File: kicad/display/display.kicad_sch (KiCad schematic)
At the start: 25 parts, among them J1 Conn. 02x12, P1 10k, P2 10k, P3 10k stereo, P4 10k, T1 2N3904, T2 2N3904, U1 4066N, U2 RC1602A

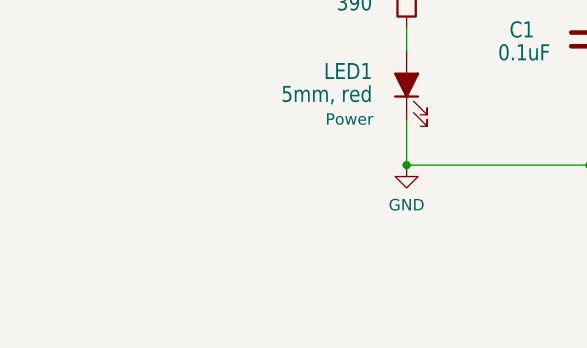
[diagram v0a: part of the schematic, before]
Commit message: Fixing mounting holes for display print
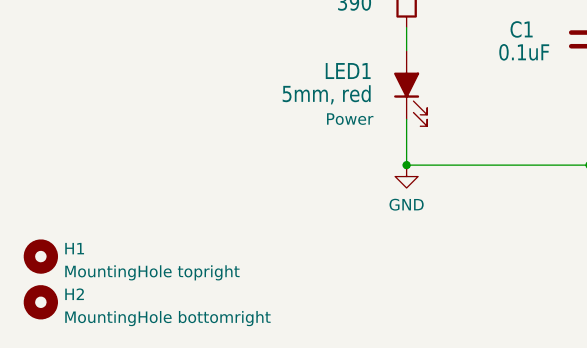
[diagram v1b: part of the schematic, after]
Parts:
- added H1: MountingHole topright, MountingHole:MountingHole_2.1mm, symbol Mechanical:MountingHole
- added H2: MountingHole bottomright, MountingHole:MountingHole_2.1mm, symbol Mechanical:MountingHole
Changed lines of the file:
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@@
     (pin "4")
+  )
+  (symbol (lib_id "Mechanical:MountingHole") (at 24.13 187.96 0) (unit 1)
+    (in_bom yes) (on_board yes) (fields_autoplaced)
+    (property "Reference" "H1" (id 0) (at 26.67 187.1253 0)
+      (effects (font (size 1.27 1.27)) (justify left))
+    )
+    (property "Value" "MountingHole topright" (id 1) (at 26.67 189.6622 0)
+      (effects (font (size 1.27 1.27)) (justify left))
+    )
+    (property "Footprint" "MountingHole:MountingHole_2.1mm" (id 2) (at 24.13 187.96 0)
+      (effects (font (size 1.27 1.27)) hide)
+    )
+    (property "Datasheet" "~" (id 3) (at 24.13 187.96 0)
+      (effects (font (size 1.27 1.27)) hide)
+    )
   )
   (symbol (lib_id "Device:R_Potentiometer") (at 41.91 107.95 0) (mirror x) (unit 1)
@@
     (pin "3")
     (pin "4")
+  )
+  (symbol (lib_id "Mechanical:MountingHole") (at 24.13 193.04 0) (unit 1)
+    (in_bom yes) (on_board yes) (fields_autoplaced)
+    (property "Reference" "H2" (id 0) (at 26.67 192.2053 0)
+      (effects (font (size 1.27 1.27)) (justify left))
+    )
+    (property "Value" "MountingHole bottomright" (id 1) (at 26.67 194.7422 0)
+      (effects (font (size 1.27 1.27)) (justify left))
+    )
+    (property "Footprint" "MountingHole:MountingHole_2.1mm" (id 2) (at 24.13 193.04 0)
+      (effects (font (size 1.27 1.27)) hide)
+    )
+    (property "Datasheet" "~" (id 3) (at 24.13 193.04 0)
+      (effects (font (size 1.27 1.27)) hide)
+    )
   )
   (symbol (lib_id "Device:R") (at 242.57 33.02 0) (mirror x) (unit 1)
@@
       (reference "C1") (unit 1) (value "0.1uF") (footprint "Capacitor_THT:C_Disc_D3.4mm_W2.1mm_P2.50mm")
     )
+    (path "/52fbbb5e-e2d2-42c1-a80c-566ffb9e6372"
+      (reference "H1") (unit 1) (value "MountingHole topright") (footprint "MountingHole:MountingHole_2.1mm")
+    )
+    (path "/a2ed2906-2e6a-49f5-b00c-a2101572ab11"
+      (reference "H2") (unit 1) (value "MountingHole bottomright") (footprint "MountingHole:MountingHole_2.1mm")
+    )
     (path "/e5041354-b711-4490-a712-dc956e45a881"

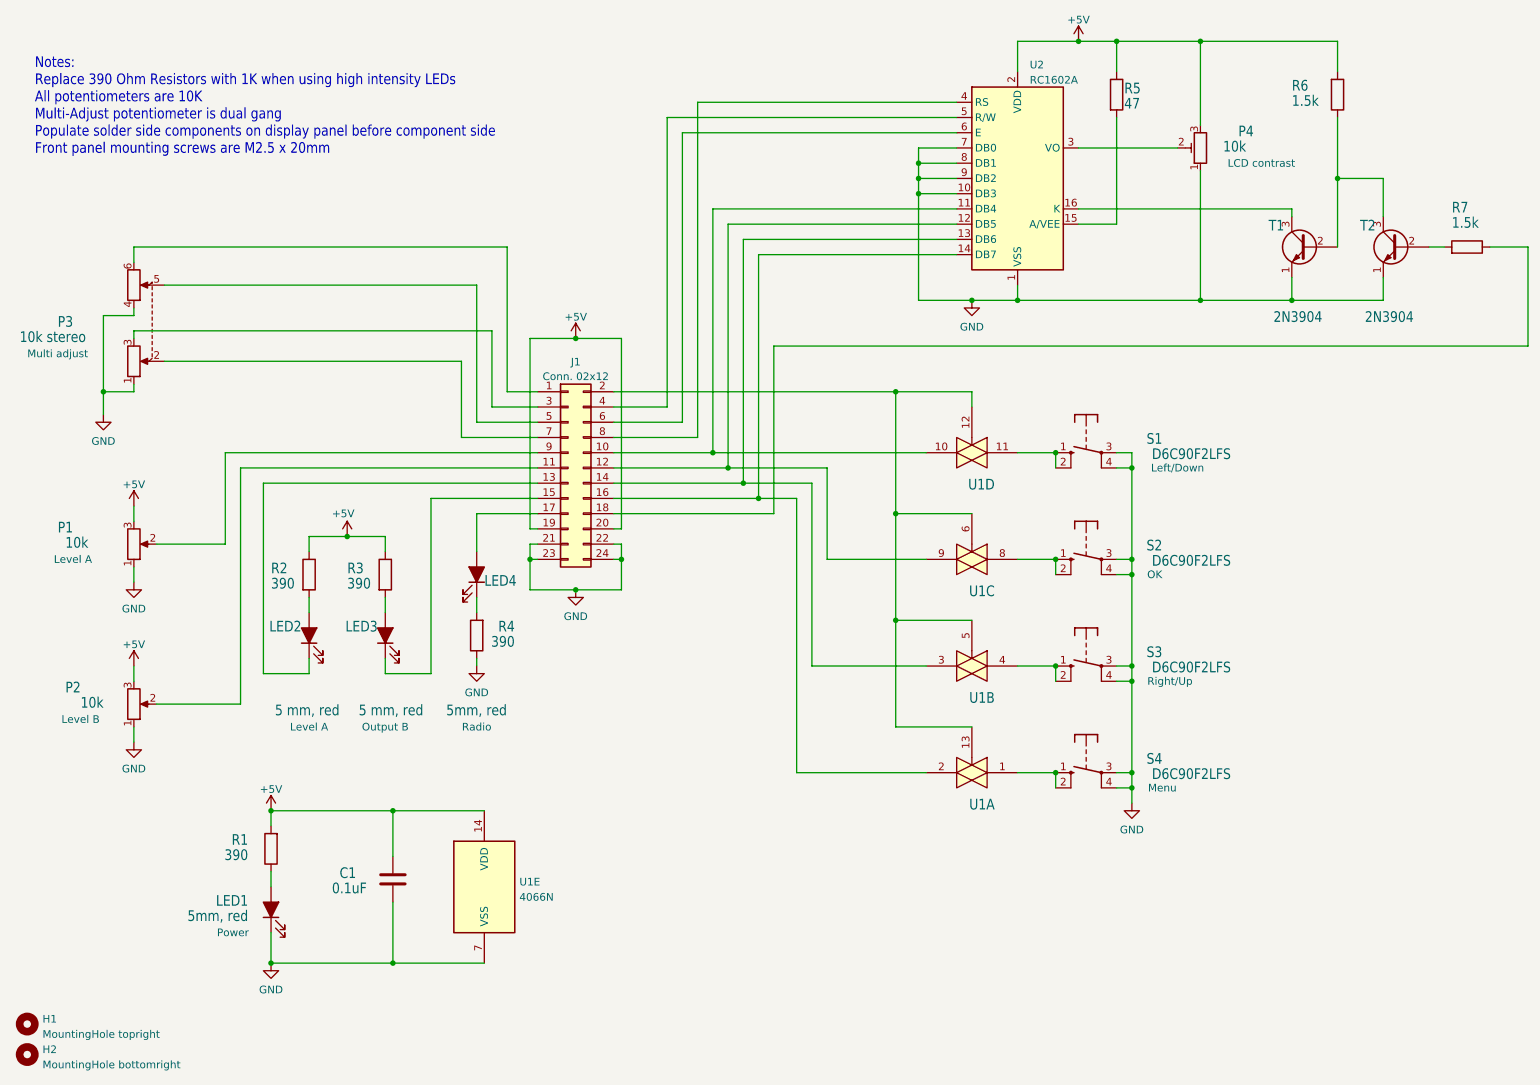
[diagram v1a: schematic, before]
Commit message: Display print is now on parity with V1.4, but has been re-routed. U3 has also been rotated 180 degrees. Some components have been moved to other places as well
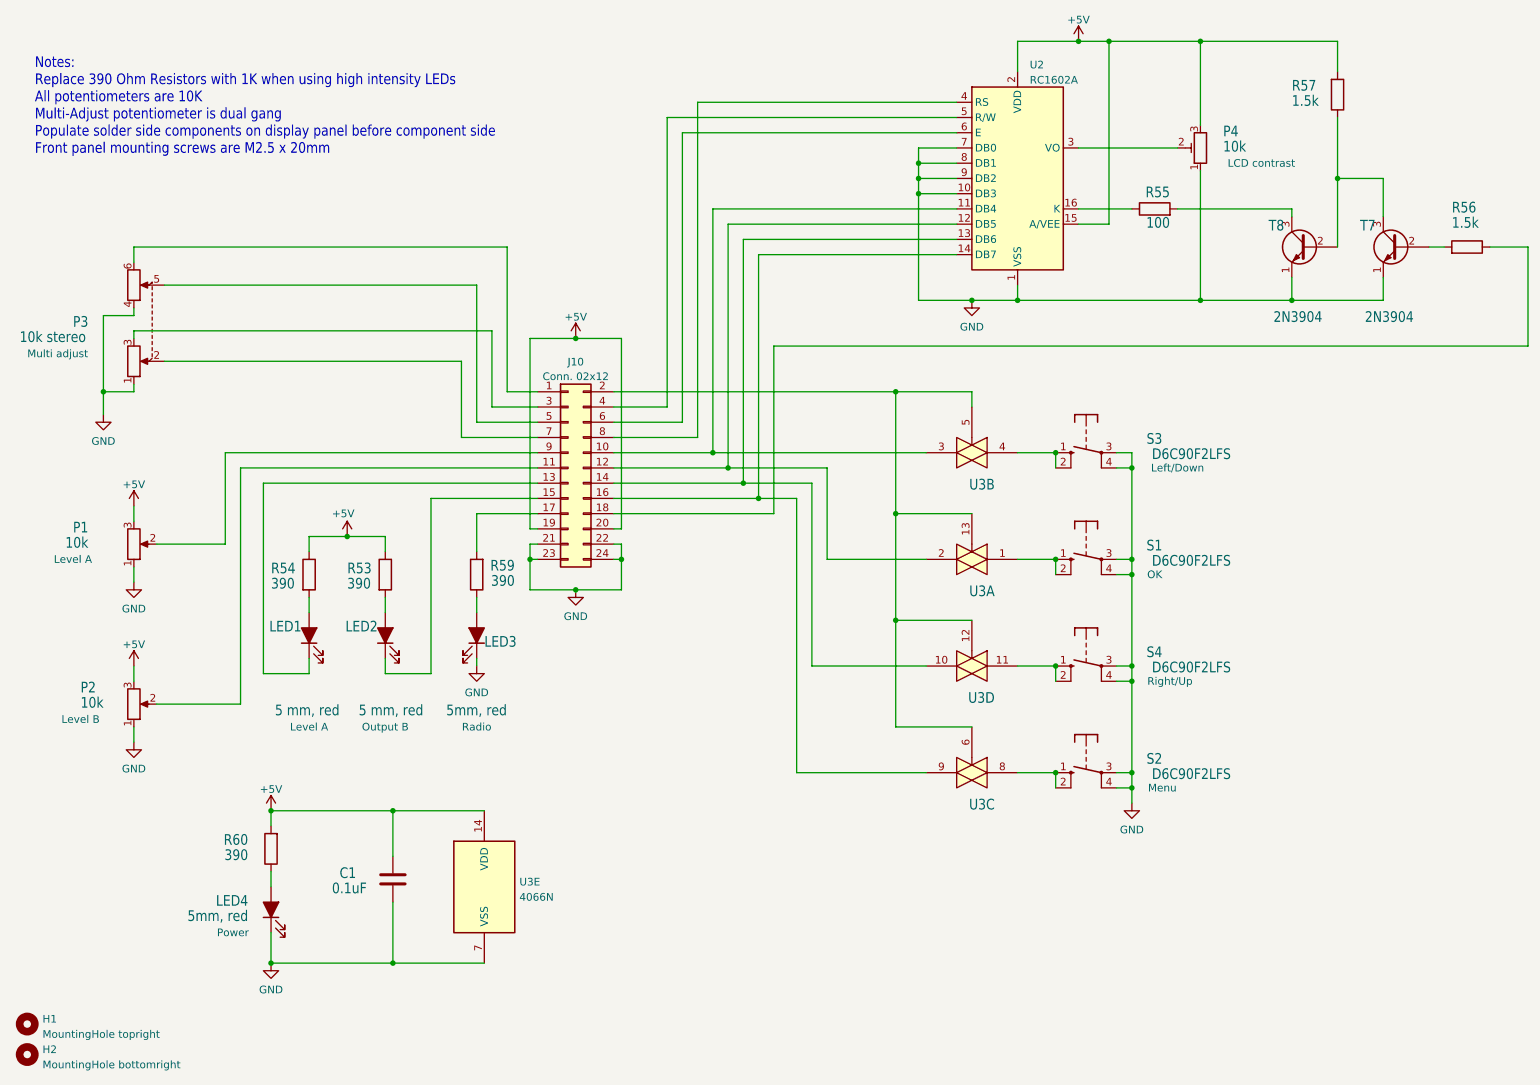
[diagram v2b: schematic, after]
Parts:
- R55: renamed from R5; value 47 -> 100
- renumbered J1 to J10, LED2 to LED1, LED3 to LED2, LED4 to LED3, LED1 to LED4, R3 to R53, R2 to R54, R7 to R56, R6 to R57, R4 to R59, R1 to R60, S2 to S1, S4 to S2, S1 to S3, S3 to S4, T2 to T7, T1 to T8, U1 to U3
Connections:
- net +5V: now also U2.15 (A/VEE); no longer R55.1
- net GND: now also LED3.1 (K); no longer R59.1
- net at R59.2: now also J10.17 (Pin_17); no longer LED3.1 (K)
- net at R55.2: now also T8.3 (C); no longer U2.15 (A/VEE)
- net at J10.10 (Pin_10), U2.11 (DB4): now also U3.3; no longer U3.10
- net at J10.12 (Pin_12), U2.12 (DB5): now also U3.2; no longer U3.9
- net at J10.14 (Pin_14), U2.13 (DB6): now also U3.10; no longer U3.3
- net at J10.16 (Pin_16), U2.14 (DB7): now also U3.9; no longer U3.2
- net at U2.16 (K): now also R55.1; no longer T8.3 (C)
- net at S4.1 (S), S4.2 (S@1): now also U3.11; no longer U3.4
- net at S1.1 (S), S1.2 (S@1): now also U3.1; no longer U3.8
- net at S2.1 (S), S2.2 (S@1): now also U3.8; no longer U3.1
- net at LED3.2 (A): now also R59.1; no longer J10.17 (Pin_17)
- net at S3.1 (S), S3.2 (S@1): now also U3.4; no longer U3.11
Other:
- title: MK-312 Display print -> MK-312BT Display print
- moved on the sheet: LED3, R55, R59, U3A, U3B, U3C, U3D

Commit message: Brought component numbers back in line with the original schematics
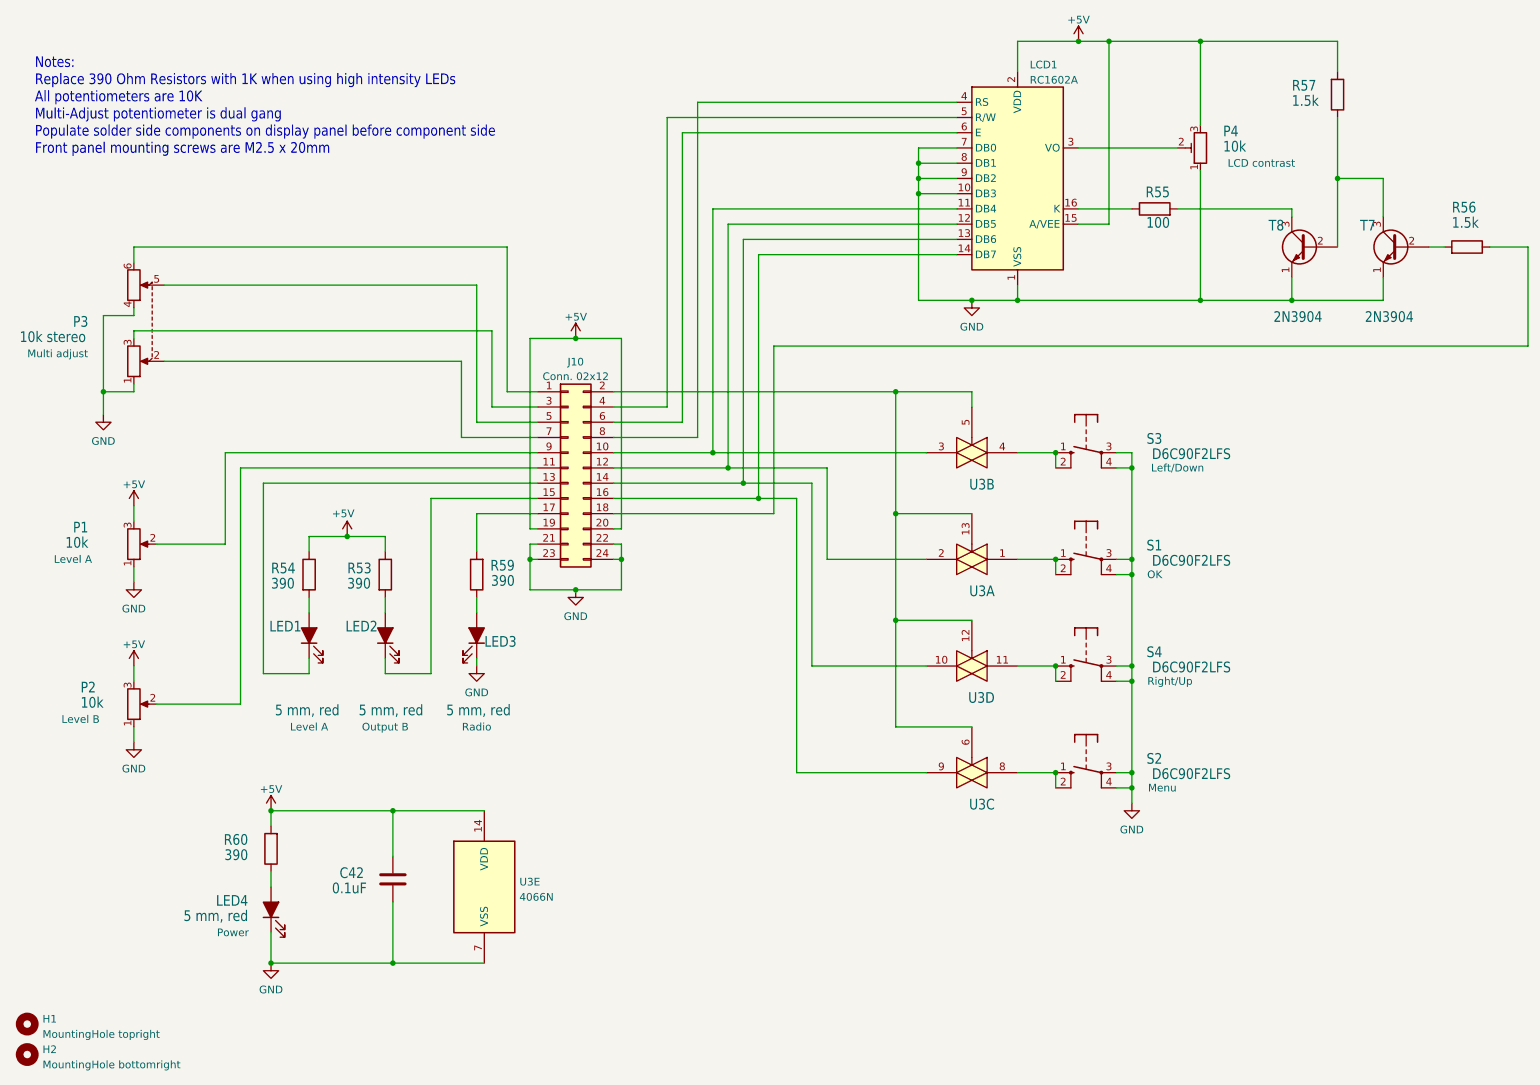
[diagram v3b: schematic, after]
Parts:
- LED3, LED4: value 5mm, red -> 5 mm, red
- renumbered C1 to C42, U2 to LCD1
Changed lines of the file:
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@@
   (symbol (lib_id "Device:C") (at 85.09 163.83 0) (unit 1)
     (in_bom yes) (on_board yes)
-    (property "Reference" "C1" (id 0) (at 76.2 163.83 0)
+    (property "Reference" "C42" (id 0) (at 76.2 163.83 0)
       (effects (font (size 1.778 1.5113)) (justify left bottom))
     )
@@
   (symbol (lib_id "Display_Character:RC1602A") (at 189.23 46.99 0) (unit 1)
     (in_bom yes) (on_board yes) (fields_autoplaced)
-    (property "Reference" "U2" (id 0) (at 191.2494 28.0502 0)
+    (property "Reference" "LCD1" (id 0) (at 191.2494 28.0502 0)
       (effects (font (size 1.27 1.27)) (justify left))
     )
@@
       (effects (font (size 1.778 1.5113)) (justify left bottom))
     )
-    (property "Value" "5mm, red" (id 1) (at 60.96 168.91 90)
+    (property "Value" "5 mm, red" (id 1) (at 60.96 168.91 90)
       (effects (font (size 1.778 1.5113)) (justify left bottom))
     )
@@
       (effects (font (size 1.778 1.5113)) (justify left bottom))
     )
-    (property "Value" "5mm, red" (id 1) (at 93.98 134.62 90)
+    (property "Value" "5 mm, red" (id 1) (at 93.98 134.62 90)
       (effects (font (size 1.778 1.5113)) (justify left bottom))
     )
@@
     )
     (path "/37d05d0c-fd2c-47ad-99b1-bd0042f10a5e"
-      (reference "C1") (unit 1) (value "0.1uF") (footprint "Capacitor_THT:C_Disc_D3.4mm_W2.1mm_P2.50mm")
+      (reference "C42") (unit 1) (value "0.1uF") (footprint "Capacitor_THT:C_Disc_D3.4mm_W2.1mm_P2.50mm")
     )
     (path "/52fbbb5e-e2d2-42c1-a80c-566ffb9e6372"
@@
       (reference "J10") (unit 1) (value "Conn. 02x12") (footprint "Connector_IDC:IDC-Header_2x12_P2.54mm_Vertical")
     )
+    (path "/49ff3ae1-ae02-4def-bf64-4b538d23f00c"
+      (reference "LCD1") (unit 1) (value "RC1602A") (footprint "Display:WC1602A")
+    )
     (path "/e5b8127c-a986-441d-9655-260089edadc4"
       (reference "LED1") (unit 1) (value "5 mm, red") (footprint "LED_THT:LED_D5.0mm")
@@
     )
     (path "/7f11bb71-0b23-427a-a835-54b1dd9e05f6"
-      (reference "LED3") (unit 1) (value "5mm, red") (footprint "LED_THT:LED_D5.0mm")
+      (reference "LED3") (unit 1) (value "5 mm, red") (footprint "LED_THT:LED_D5.0mm")
     )
     (path "/5a196dae-b249-4e08-89df-c3de0945af88"
-      (reference "LED4") (unit 1) (value "5mm, red") (footprint "LED_THT:LED_D5.0mm")
+      (reference "LED4") (unit 1) (value "5 mm, red") (footprint "LED_THT:LED_D5.0mm")
     )
     (path "/566b906f-57c5-4d05-84c1-6fa6c729218f"
@@
       (reference "T8") (unit 1) (value "2N3904") (footprint "Package_TO_SOT_THT:TO-92_Inline")
     )
-    (path "/49ff3ae1-ae02-4def-bf64-4b538d23f00c"
-      (reference "U2") (unit 1) (value "RC1602A") (footprint "Display:WC1602A")
-    )
     (path "/73fcf29c-182d-4f9a-9237-8fd20f0b67be"

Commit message: Two small fixups for the display & frontend. Made mounting holes in display PCB larger. Moved LCD window slightly to the right on the front panel.
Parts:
- H1, H2: footprint MountingHole:MountingHole_2.1mm -> MountingHole:MountingHole_2.5mm
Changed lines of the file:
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@@
   (title_block
     (title "MK-312BT Display print")
-    (date "2022-08-09")
-    (rev "1.4-Chi")
+    (date "2022-09-05")
+    (rev "1.4.1-Chi")
   )
   (junction (at 172.72 49.53) (diameter 0) (color 0 0 0 0)
@@
       (effects (font (size 1.27 1.27)) (justify left))
     )
-    (property "Footprint" "MountingHole:MountingHole_2.1mm" (id 2) (at 24.13 187.96 0)
+    (property "Footprint" "MountingHole:MountingHole_2.5mm" (id 2) (at 24.13 187.96 0)
       (effects (font (size 1.27 1.27)) hide)
     )
@@
       (effects (font (size 1.27 1.27)) (justify left))
     )
-    (property "Footprint" "MountingHole:MountingHole_2.1mm" (id 2) (at 24.13 193.04 0)
+    (property "Footprint" "MountingHole:MountingHole_2.5mm" (id 2) (at 24.13 193.04 0)
       (effects (font (size 1.27 1.27)) hide)
     )
@@
     )
     (path "/52fbbb5e-e2d2-42c1-a80c-566ffb9e6372"
-      (reference "H1") (unit 1) (value "MountingHole topright") (footprint "MountingHole:MountingHole_2.1mm")
+      (reference "H1") (unit 1) (value "MountingHole topright") (footprint "MountingHole:MountingHole_2.5mm")
     )
     (path "/a2ed2906-2e6a-49f5-b00c-a2101572ab11"
-      (reference "H2") (unit 1) (value "MountingHole bottomright") (footprint "MountingHole:MountingHole_2.1mm")
+      (reference "H2") (unit 1) (value "MountingHole bottomright") (footprint "MountingHole:MountingHole_2.5mm")
     )
     (path "/e5041354-b711-4490-a712-dc956e45a881"
